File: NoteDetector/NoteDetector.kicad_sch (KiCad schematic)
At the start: 47 parts, among them J1 Conn_02x03, J3 Conn_01x01, J4 Conn_01x01, Q1 Q_NMOS_DGS, U2 OPAMP, U3 ATtiny1614-SS

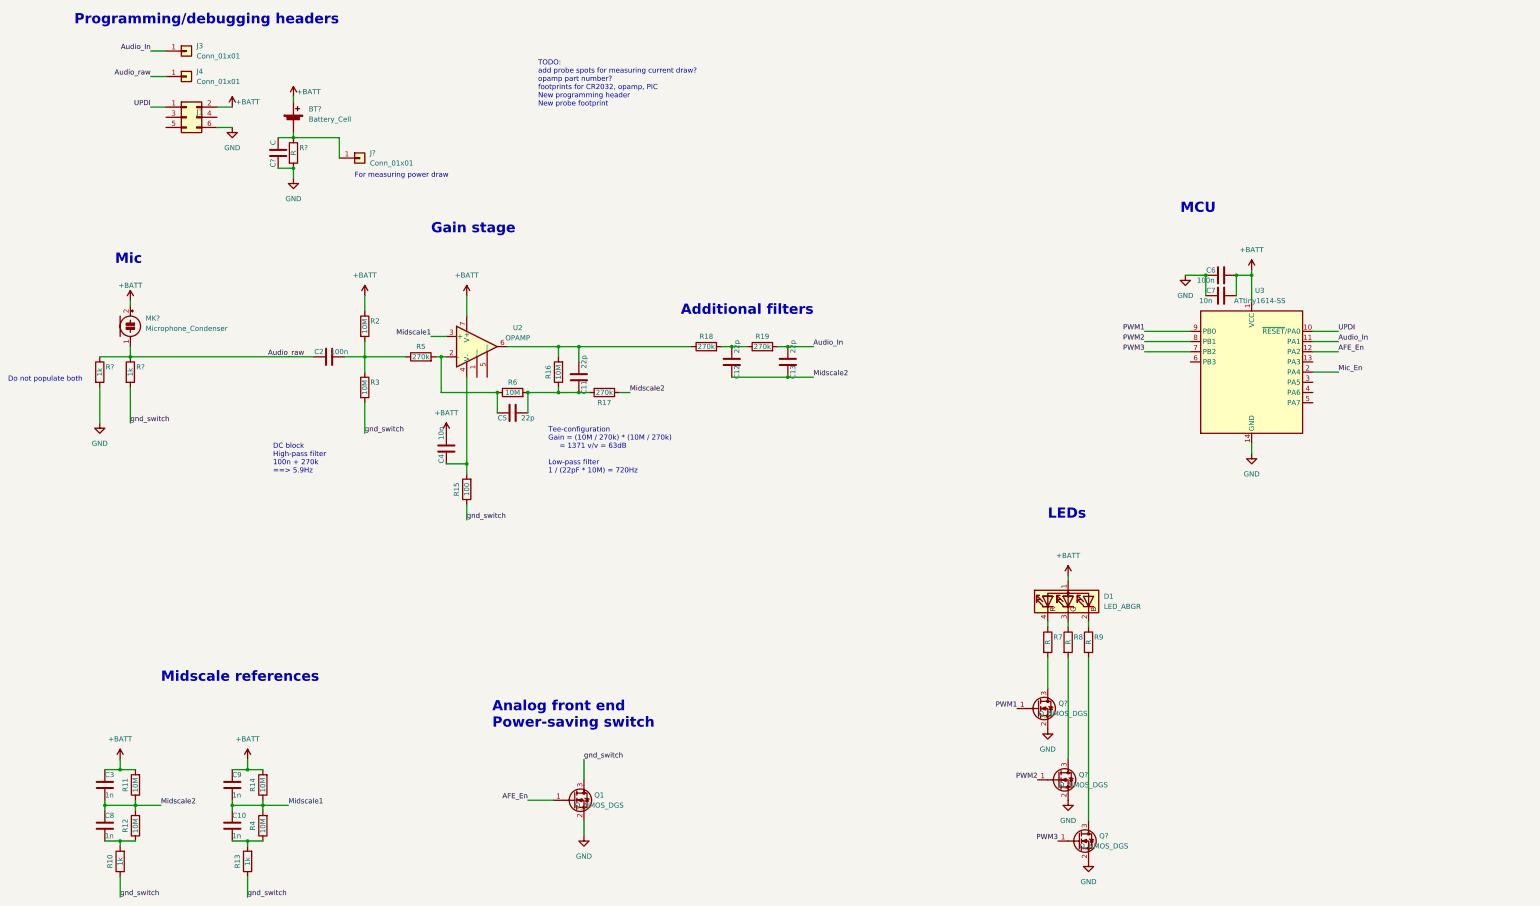
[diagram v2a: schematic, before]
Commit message: Save work; Added a new schematic symbol for the PIC18F06Q41; new footprint for the MO063602-1 condenser mic
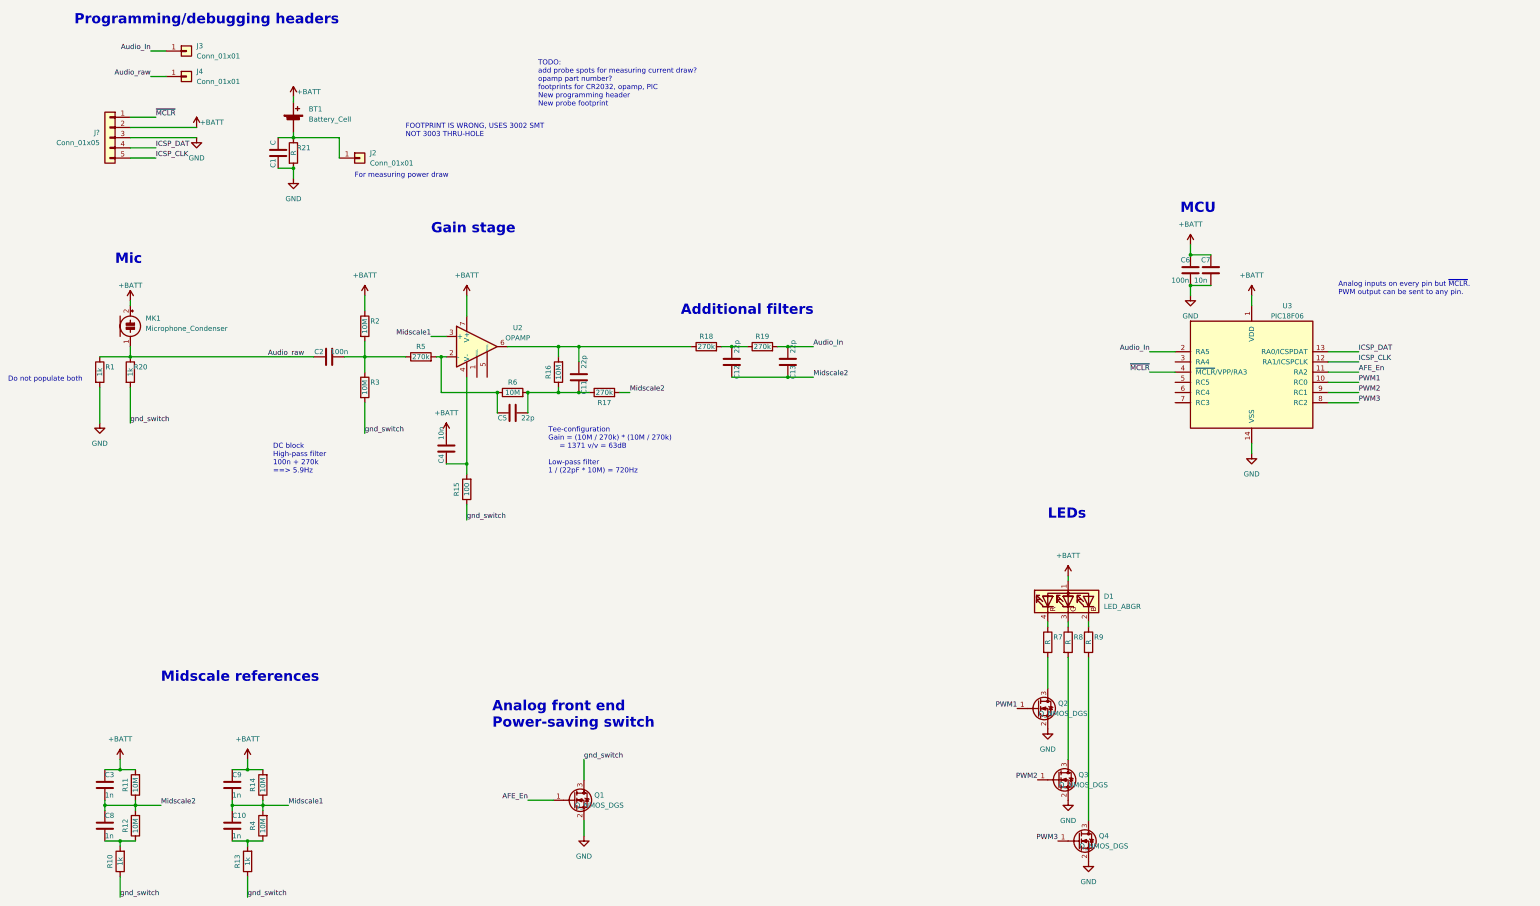
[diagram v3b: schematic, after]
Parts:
- removed J1: Conn_02x03, Connector_PinSocket_2.54mm:PinSocket_2x03_P2.54mm_Vertical, symbol Connector_Generic:Conn_02x03_Odd_Even
- added J?: Conn_01x05, symbol Connector_Generic:Conn_01x05
- BT1: renamed from BT?; footprint (none) -> Battery:BatteryHolder_Keystone_3002_1x2032; Part Number (none) -> Keystone 3003
- MK1: renamed from MK?; footprint (none) -> User:ElectretCondenserMic_SMT_MO063602-1; Part Number (none) -> MO063602-1
- U3: value ATtiny1614-SS -> PIC18F06; footprint Package_SO:SOIC-14_3.9x8.7mm_P1.27mm -> Package_SO:TSSOP-14_4.4x5mm_P0.65mm; symbol MCU_Microchip_ATtiny:ATtiny1614-SS -> user:PIC18F06Q41; Alternate (none) -> PIC18F06Q40-E/ST; Part Number (none) -> PIC18F06Q41-E/ST
- gave numbers to parts that had none: 8
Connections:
- net Mic_En is gone; now on net Audio_In: U3.2 (RA5)
- net UPDI is gone; now on net PWM1: U3.10 (RC0)
- net +BATT: now also J?.2 (Pin_2)
- net AFE_En: now also U3.11 (RA2); no longer U3.12 (PA2)
- net Audio_In: no longer U3.11 (PA1)
- net GND: now also J?.3 (Pin_3)
- net PWM1: no longer U3.9 (PB0)
- net PWM2: now also U3.9 (RC1); no longer U3.8 (PB1)
- net PWM3: now also U3.8 (RC2); no longer U3.7 (PB2)
- net ICSP_DAT: now reaches U3.13 (RA0/ICSPDAT)
- net ICSP_DAT: now also J?.4 (Pin_4)
- net ~{MCLR}: now reaches U3.4 (~{MCLR}/VPP/RA3)
- net ~{MCLR}: now also J?.1 (Pin_1)
- new net ICSP_CLK: J?.5 (Pin_5), U3.12 (RA1/ICSPCLK)
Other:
- note added: "Analog inputs on every pin but ~{MCLR}. PWM output can be sent to any pin."
- note added: "FOOTPRINT IS WRONG, USES 3002 SMT NOT 3003 THRU-HOLE"
- moved on the sheet: C6, C7, U3

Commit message: save work: new layout almost done
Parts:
- removed BT1: Battery_Cell, Battery:BatteryHolder_Keystone_3002_1x2032, symbol Device:Battery_Cell
- removed C1: C, Capacitor_SMD:C_0603_1608Metric, symbol Device:C
- removed R21: R, Resistor_SMD:R_0603_1608Metric, symbol Device:R
- added C13, C14, C15: 1u, Capacitor_SMD:C_0603_1608Metric, symbol Device:C
- added J5: Conn_01x01, TestPoint:TestPoint_Loop_D2.50mm_Drill1.0mm, symbol Connector_Generic:Conn_01x01
- J1: renamed from J?; footprint (none) -> Connector_PinHeader_1.27mm:PinHeader_2x03_P1.27mm_Vertical; symbol Connector_Generic:Conn_01x05 -> Connector_Generic:Conn_01x06
- J2: renamed from J3; footprint TestPoint:TestPoint_Loop_D2.50mm_Drill1.0mm -> TestPoint:TestPoint_Pad_D1.0mm; PN 5000 (Keystone) -> (none)
- J3: renamed from J4; footprint TestPoint:TestPoint_Loop_D2.50mm_Drill1.0mm -> TestPoint:TestPoint_Pad_D1.0mm; PN 5000 (Keystone) -> (none)
- U1: renamed from U2; footprint Package_SO:SOIC-8_3.9x4.9mm_P1.27mm -> Package_TO_SOT_SMD:SOT-23-5; symbol Amplifier_Operational:LM741 -> Amplifier_Operational:MCP6L91T-EOT; PN MCP6061-E/SN -> MCP6061T-E/OT
- renumbered C3 to C1, C13 to C10, C6 to C11, C7 to C12, C8 to C2, C9 to C3, C10 to C4, C2 to C5, C4 to C6, C5 to C7, C11 to C8, C12 to C9, J2 to J4, R3 to R10, R5 to R11, R15 to R12, R6 to R13, R16 to R14, R17 to R15, R18 to R16, R19 to R17, R7 to R18, R8 to R19, R10 to R2, R9 to R20, R20 to R3, R11 to R4, R12 to R5, R13 to R6, R14 to R7, R4 to R8, R2 to R9, U3 to U2
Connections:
- net +BATT: now also J4.1 (Pin_1), U1.5 (V+); no longer U1.7 (V+)
- net GND: now also C13.2, C14.2, C15.2, J5.1 (Pin_1)
- net at C8.1, R14.2, R16.1: now also U1.1; no longer U1.6
- net at C7.2, R11.2, R13.1: now also U1.4 (-); no longer U1.2 (-)
- net at C6.2, R12.2: now also U1.2 (V-); no longer U1.4 (V-)
- net at D1.2 (BK), R20.1: now also C15.1
- net at D1.3 (GK), R19.1: now also C14.1
- net at D1.4 (RK), R18.1: now also C13.1
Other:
- note added: "Analog test points"
- note added: "Battery header"
- note added: "ICSP header"
- note added: "TODO: check "high power" LED switching lines"
- note removed: "FOOTPRINT IS WRONG, USES 3002 SMT NOT 3003 THRU-HOLE"
- note removed: "For measuring power draw"
- note removed: "Programming/debugging headers"
- note removed: "TODO: add probe spots for measuring current draw? opamp part number? footprints for CR2032, opamp, PIC New programming header New probe footprint"
- moved on the sheet: J2, J3, J4, Q2, Q3, Q4, R19

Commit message: rev2 board layout done
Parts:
- J1: footprint Connector_PinHeader_1.27mm:PinHeader_2x03_P1.27mm_Vertical -> (none)
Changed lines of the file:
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@@
       (effects (font (size 1.27 1.27)) (justify left) hide)
     )
-    (property "Footprint" "Connector_PinHeader_1.27mm:PinHeader_2x03_P1.27mm_Vertical" (id 2) (at 22.86 45.72 0)
+    (property "Footprint" "" (id 2) (at 22.86 45.72 0)
       (effects (font (size 1.27 1.27)) hide)
     )
@@
     )
     (path "/0dfca3c8-1ecc-44e1-81b5-40a2d43c452a"
-      (reference "J1") (unit 1) (value "Conn_01x05") (footprint "Connector_PinHeader_1.27mm:PinHeader_2x03_P1.27mm_Vertical")
+      (reference "J1") (unit 1) (value "Conn_01x05") (footprint "")
     )
     (path "/e72eb35d-61d7-4c28-a823-6375b6639f62"

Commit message: Added programming bed PCB; moved PCB programming pads; added CR2032 battery holder; todo: fix silkscreen
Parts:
- removed J1: Conn_01x05, symbol Connector_Generic:Conn_01x06
- added BT1: CR2032Holder, User:BH-25C-1, symbol Device:Battery_Cell
- added J1, J6, J7: Conn_01x01, TestPoint:TestPoint_Pad_D1.0mm, symbol Connector_Generic:Conn_01x01
- C1, C2, C3, C4: Alternate (none) -> CL10C102JB8NNND; Part Number (none) -> GRM1885C1H102JA01D
- C10, C7, C8, C9: Alternate (none) -> CL10C220JB8NNNC; Part Number (none) -> 06035A220JAT2A
- C11, C5: Part Number (none) -> CL10B104JB8NNNC
- C12, C6: Part Number (none) -> 0603B103J500CT
- C13, C14, C15: Part Number (none) -> CL10A105KO8NNND
- D1: PN CLMVC-FKA-CL1D1L71BB7C3C3 -> (none); Part Number (none) -> CLMVC-FKA-CL1D1L71BB7C3C3
- J2, J3: Part Number (none) -> none
- J4, J5: footprint TestPoint:TestPoint_Loop_D2.50mm_Drill1.0mm -> TestPoint:TestPoint_Pad_D1.0mm; PN 5000 (Keystone) -> (none); Part Number (none) -> none
- Q1: Alternate (none) -> NX7002AKAR; PN RUC002N05HZGT116 -> (none); Part Number (none) -> T2N7002AK,LM
- Q2, Q3, Q4: Alternate (none) -> NX7002AKAR; Part Number (none) -> T2N7002AK,LM
- R1, R2, R3, R6: Part Number (none) -> CRCW06031K00FKEAC
- R10, R13, R14, R4, R5, R7, R8, R9: Alternate (none) -> RMCF0603FT10M0; PN RMCF0603FT10M0 -> (none); Part Number (none) -> WR06W1005FTL
- R11: Alternate (none) -> WR06X2703FTL; Part Number (none) -> RC0603FR-07270KL
- R12: Part Number (none) -> CRG0603F100R
- R15, R16, R17: Alternate (none) -> WR06X2703FTL; PN RMCF0603FT100K -> (none); Part Number (none) -> RC0603FR-07270KL
- R18: value R -> 1k; Part Number (none) -> CRCW06031K00FKEAC
- R19: value R -> 1.4k; Part Number (none) -> CR0603-FX-1401ELF
- R20: value R -> 1.5k; Part Number (none) -> RC0603JR-131K5L
- U1: Alternate (none) -> MCP6231T-E/OT; PN MCP6061T-E/OT -> (none); Part Number (none) -> MCP6061T-E/OT
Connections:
- net +BATT: now also BT1.1 (+)
- net GND: now also BT1.2 (-)
- net ICSP_CLK: now also J7.1 (Pin_1)
- net ICSP_DAT: now also J6.1 (Pin_1)
- net ~{MCLR}: now also J1.1 (Pin_1)
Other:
- note added: "Battery holder"
- note added: "TODO: Add gate resistors"
- note removed: "Battery header"

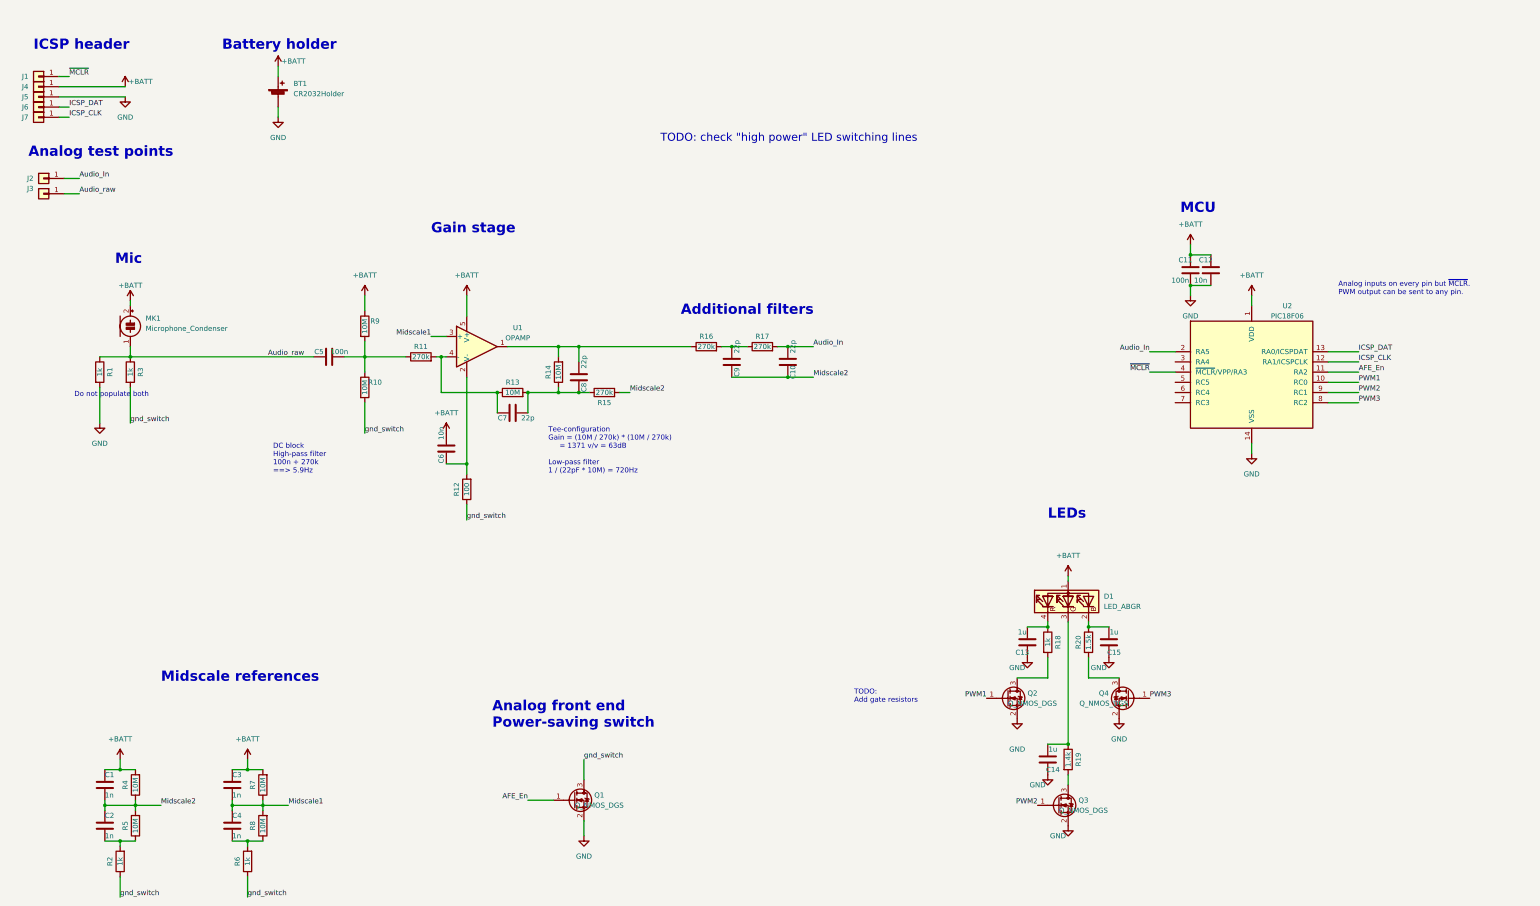
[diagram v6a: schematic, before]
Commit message: Updated BOM, moved programming pads outside of CR2032 battery holder coverage; board layout not finished
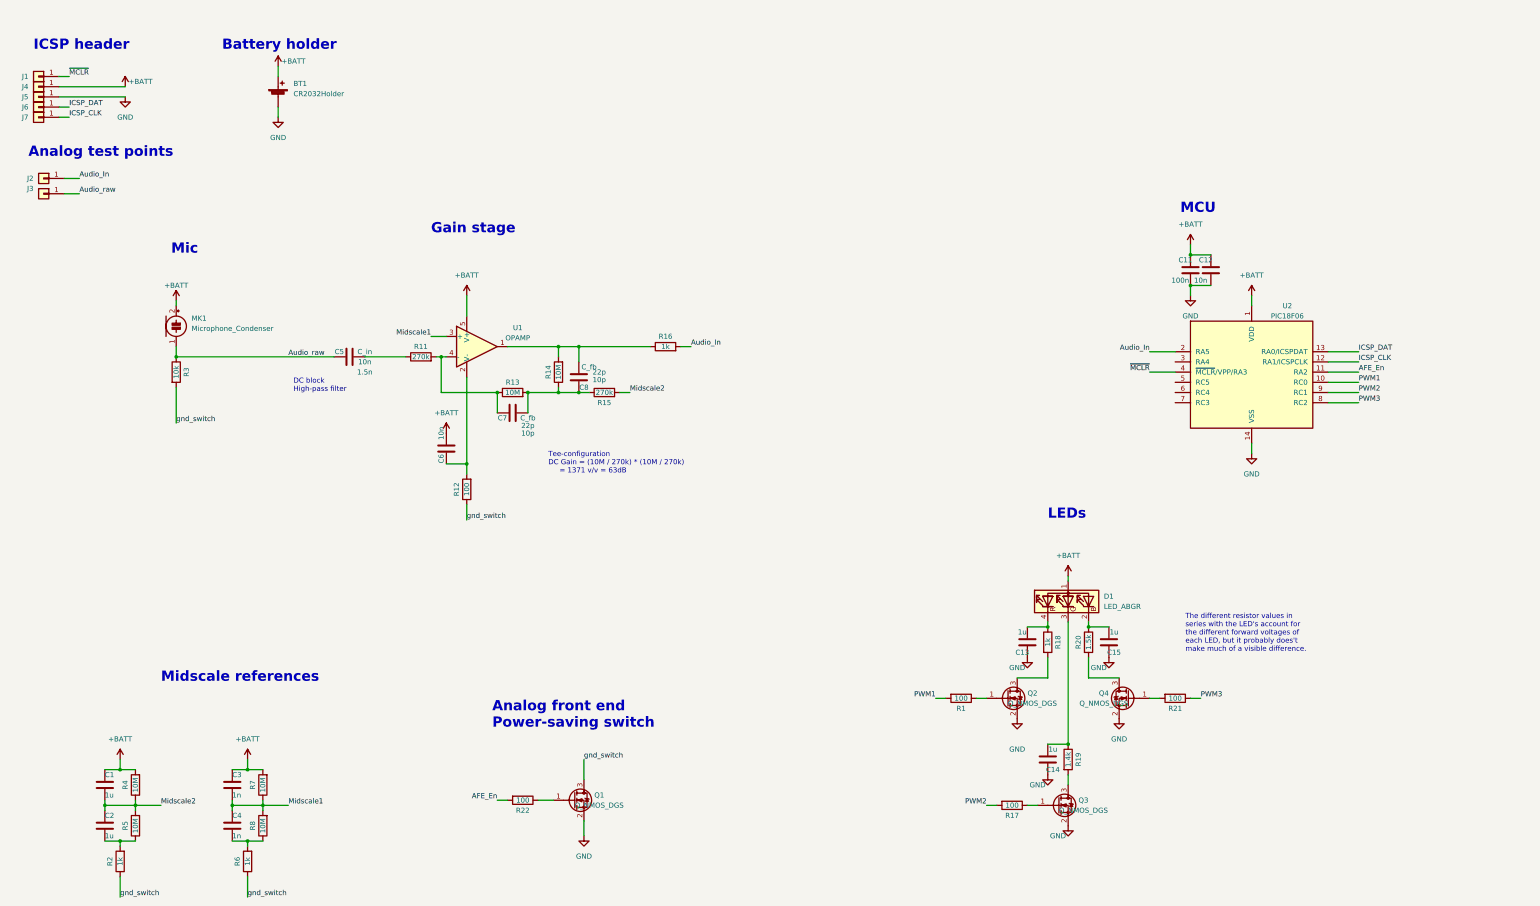
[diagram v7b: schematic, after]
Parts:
- removed C10, C9: 22p, Capacitor_SMD:C_0603_1608Metric, symbol Device:C
- removed R10, R9: 10M, Resistor_SMD:R_0603_1608Metric, symbol Device:R
- added R21, R22: 100, Resistor_SMD:R_0603_1608Metric, symbol Device:R
- C1, C2: value 1n -> 1u; Alternate CL10C102JB8NNND -> (none); Part Number GRM1885C1H102JA01D -> CL10A105KO8NNND
- C3, C4: Alternate CL10C102JB8NNND -> (none)
- C5: value 100n -> C_in; Part Number CL10B104JB8NNNC -> (none); Part Number Alt 1 (none) -> CL10B104JB8NNNC; Val1 (none) -> 10n; Val2 (none) -> 1.5n
- C7, C8: value 22p -> C_fb; Alternate CL10C220JB8NNNC -> (none); Part Number 06035A220JAT2A -> (none); Part Number Alt 1 (none) -> 06035A220JAT2A; Val1 (none) -> 22p; Val2 (none) -> 10p
- Q1, Q2, Q3, Q4: Alternate NX7002AKAR -> (none)
- R1: value 1k -> 100; Part Number CRCW06031K00FKEAC -> CRG0603F100R
- R11, R15: Alternate WR06X2703FTL -> (none)
- R13, R14, R4, R5, R7, R8: Alternate RMCF0603FT10M0 -> (none)
- R16: value 270k -> 1k; Alternate WR06X2703FTL -> (none); Part Number RC0603FR-07270KL -> CRCW06031K00FKEAC
- R17: value 270k -> 100; Alternate WR06X2703FTL -> (none); Part Number RC0603FR-07270KL -> CRG0603F100R
- R3: value 1k -> 10k; Part Number CRCW06031K00FKEAC -> (none)
- U1: Alternate MCP6231T-E/OT -> (none); Part Number MCP6061T-E/OT -> MCP6061T-E/OT or MCP6231T-E/OT
- U2: Alternate PIC18F06Q40-E/ST -> (none); Part Number PIC18F06Q41-E/ST -> PIC18F06Q41-E/ST or PIC18F06Q40-E/ST
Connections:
- net AFE_En: now also R22.2; no longer Q1.1 (G)
- net Audio_In: now also R16.2; no longer R17.2
- net Audio_raw: no longer R1.1
- net GND: no longer R1.2
- net PWM1: now also R1.2; no longer Q2.1 (G)
- net PWM2: now also R17.2; no longer Q3.1 (G)
- net PWM3: now also R21.1; no longer Q4.1 (G)
- net at R17.1: now also Q3.1 (G); no longer R16.2
- new net: Q1.1 (G), R22.1
- new net: Q4.1 (G), R21.2
- new net: Q2.1 (G), R1.1
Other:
- note added: "DC block High-pass filter"
- note added: "Tee-configuration DC Gain = (10M / 270k) * (10M / 270k) = 1371 v/v = 63dB"
- note added: "The different resistor values in series with the LED's account for the different forward voltages of each LED, but it probably does't make much of a visible difference."
- note removed: "Additional filters"
- note removed: "Analog inputs on every pin but ~{MCLR}. PWM output can be sent to any pin."
- note removed: "DC block High-pass filter 100n + 270k ==> 5.9Hz"
- note removed: "Do not populate both"
- note removed: "TODO: Add gate resistors"
- note removed: "TODO: check "high power" LED switching lines"
- note removed: "Tee-configuration Gain = (10M / 270k) * (10M / 270k) = 1371 v/v = 63dB Low-pass filter 1 / (22pF * 10M) = 720Hz"
- moved on the sheet: C5, MK1, R16, R3

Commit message: Added BOM; added programming bed rev1 layout
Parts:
- R3: Part Number (none) -> ERJ-3GEYJ103V
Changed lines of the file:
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@@
       (effects (font (size 1.27 1.27)) hide)
     )
-    (property "Part Number" "" (id 5) (at 57.15 114.3 0)
+    (property "Part Number" "ERJ-3GEYJ103V" (id 5) (at 57.15 114.3 0)
       (effects (font (size 1.27 1.27)) hide)
     )
